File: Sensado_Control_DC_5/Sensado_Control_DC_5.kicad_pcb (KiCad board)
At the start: 2 copper layers, 100 x 100 mm, 104 parts, among them J1 Jumper, J2 Jumper, J3 Jumper, P1 R_FUENTE_CON, P10 GPIO, P11 TOR_4, P12 TOR_2, P13 TOR_1, P14 TOR_3, P2 I_+, P3 I_-, P4 POWER, P5 RS-232, P6 I2C, P7 SPI, P8 GND_REG, P9 RESET, Q1 NMOS, Q10 PMOS, Q11 NMOS, Q12 NMOS, Q13 NMOS, Q14 PMOS, Q15 PMOS, Q16 PMOS, Q2 NMOS, Q3 NMOS, Q4 NMOS, Q5 NMOS, Q6 PMOS, Q7 PMOS, Q8 PMOS, Q9 PMOS, U1 Atmega328PA, U2 ACS_712, U3 LD1117S50TR_FINAL, Y1 XRCHA_16M

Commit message: Version para placa
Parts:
- added W1: TEST_1P, Measurement_Points:Measurement_Point_Round-TH_Small, F.Cu at (97.9, 68.4)
- added W2: TEST_1P, Measurement_Points:Measurement_Point_Round-TH_Small, F.Cu at (95.5, 90.4)
- added W3: TEST_1P, Measurement_Points:Measurement_Point_Round-TH_Small, F.Cu at (138.4, 70.6)
- added W4: TEST_1P, Measurement_Points:Measurement_Point_Round-TH_Small, F.Cu at (138.5, 83.1)
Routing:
- net /GND: track 312.5 -> 334.1 mm, vias 68 -> 72
- net /5V: track 220.9 -> 224.5 mm
- net /VOUT: track 495.2 -> 498.0 mm
- net /VFB: track 158.9 -> 161.5 mm
- net /V_FUENTE: track 31.1 -> 33.1 mm

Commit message: Capacitor DTR, Jumper Reset
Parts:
- added C10: 0,1uF, Capacitors_SMD:C_0805_HandSoldering, F.Cu at (172.6, 122.4)
- added P15: J_RESET, Socket_Strips:Socket_Strip_Straight_1x01_Pitch2.54mm, F.Cu at (176.6, 126.2)
- P5: footprint Socket_Strips:Socket_Strip_Straight_1x03_Pitch2.54mm -> Socket_Strips:Socket_Strip_Straight_1x04_Pitch2.54mm
- moved P9 3.76 mm to (172.9, 126.2)
- moved P5 2.54 mm to (176.6, 122.4)
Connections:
- P5 pad 1: /RXD -> Net-(C10-Pad1)
- P5 pad 2: /TXD -> /RXD
- P5 pad 3: /GND -> /TXD
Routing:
- net /GND: track 334.1 -> 372.0 mm, vias 72 -> 79
- net Net-(C10-Pad1): track 0.00 -> 2.79 mm
- net /SDA: track 16.5 -> 17.4 mm
- net /RESET: track 38.1 -> 37.3 mm
- net /SCL: track 25.4 -> 25.9 mm

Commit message: Logos y Nombre de Placa
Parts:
- added G***: LOGO, Logos_Fuentes:SBS, F.Cu at (126.8, 131.9)
- added G***: LOGO, Logos_Fuentes:CMOS, F.Cu at (92.6, 96.5)
- added G***: LOGO, Logos_Fuentes:UIS, F.Cu at (92.2, 107.2)
- added G***: LOGO, Logos_Fuentes:Colombia, F.Cu at (92.4, 116.8)
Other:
- board text added: "5 DC CONTROL"

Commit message: Vias para toda PCB
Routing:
- net /GND: track 372.0 -> 1306.1 mm, vias 79 -> 345
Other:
- board text added: "005 DC CONTROL"
- board text removed: "5 DC CONTROL"

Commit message: Archivo .zip actualizado de Gerbers
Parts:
- removed G***: LOGO, Logos_Fuentes:SBS
- removed G***: LOGO, Logos_Fuentes:CMOS
- removed G***: LOGO, Logos_Fuentes:UIS
- removed G***: LOGO, Logos_Fuentes:Colombia
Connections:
- net Net-(P15-Pad1) renamed /AGND
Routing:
- net /AGND: track 0.00 -> 4.22 mm, vias 0 -> 1

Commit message: Resistencias de pull up quitadas
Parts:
- removed R42, R44: 10K, Resistors_SMD:R_0805_HandSoldering
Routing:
- net /5V: track 224.5 -> 218.5 mm, vias 18 -> 19
- net /SDA_E: track 13.6 -> 10.4 mm
- net /GND: track 1306.1 -> 1309.1 mm, vias 345 -> 347
- net /SCL_E: track 11.7 -> 10.7 mm
- net /VCONTROL_7: track 98.5 -> 97.9 mm

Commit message: Capacitor del Cristal 0402 cambiados
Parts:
- C7, C8: footprint Capacitors_SMD:C_0805_HandSoldering -> Capacitors_SMD:C_0402
- moved C7 0.95 mm to (140.0, 137.3)
- moved C8 0.94 mm to (140.0, 140.0)
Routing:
- net /GND: track 1309.1 -> 1331.6 mm, vias 347 -> 354

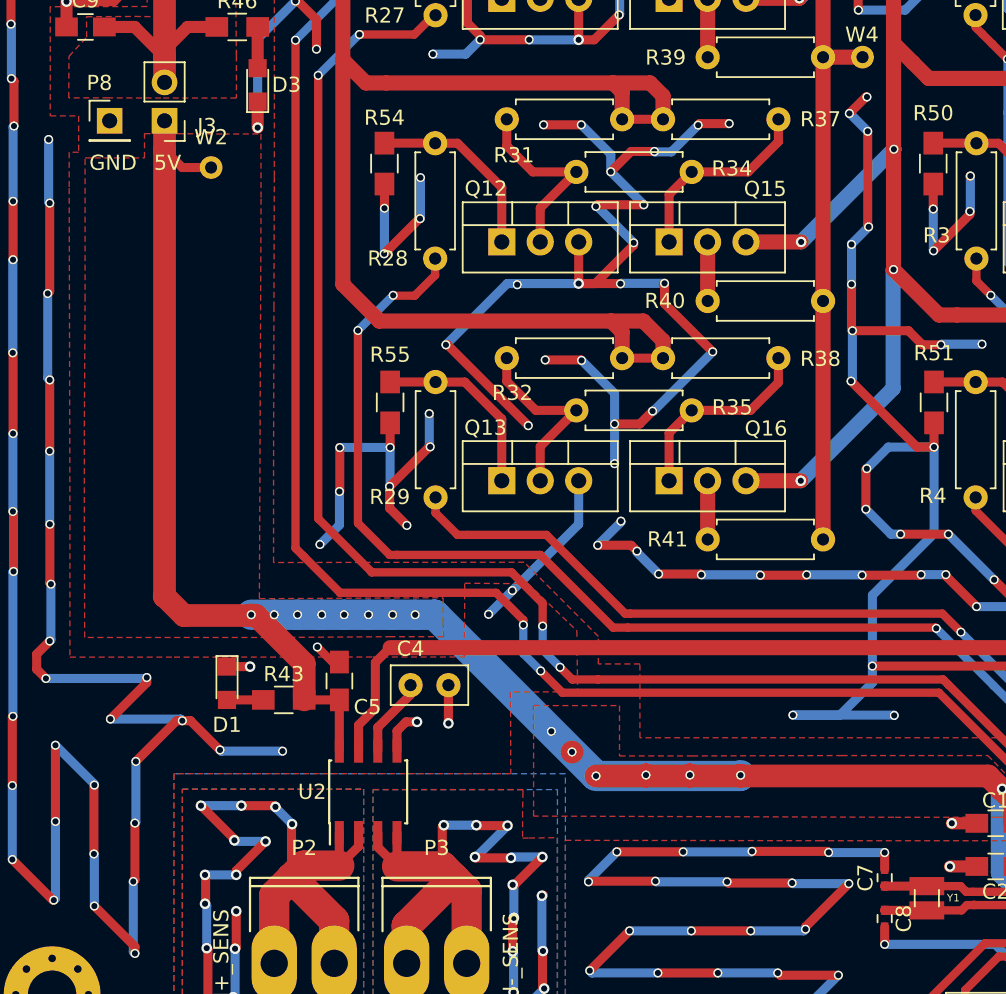
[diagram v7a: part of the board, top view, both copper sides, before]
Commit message: Nombre de Colombia añadido
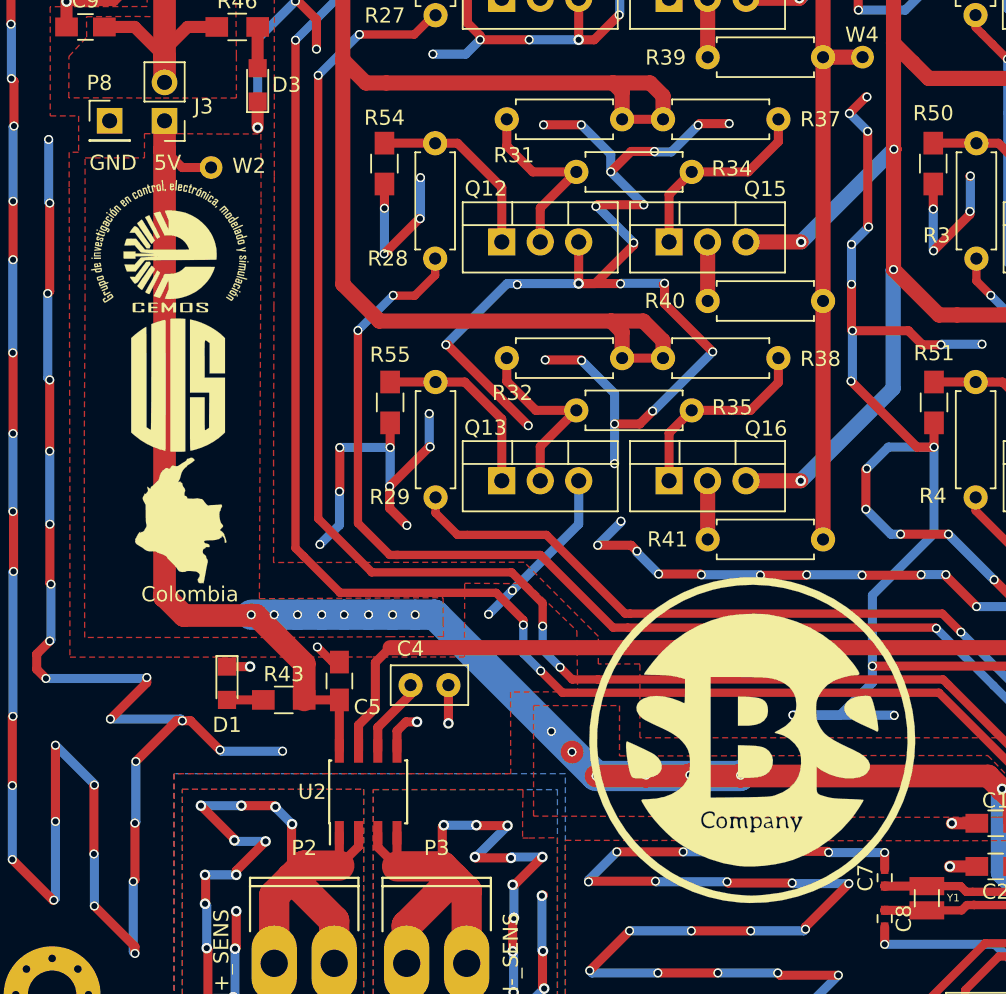
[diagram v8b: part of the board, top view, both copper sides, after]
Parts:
- added G***: LOGO, Logos_Fuentes:CMOS, F.Cu at (92.8, 95.5)
- added G***: LOGO, Logos_Fuentes:UIS, F.Cu at (93.3, 104.7)
- added G***: LOGO, Logos_Fuentes:Colombia, F.Cu at (93.5, 113.8)
- added G***: LOGO, Logos_Fuentes:SBS_22mm, F.Cu at (131.3, 128.2)
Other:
- board text added: "Colombia"
